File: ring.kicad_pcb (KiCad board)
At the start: 2 copper layers, 38 x 10 mm, 29 parts, among them J1 5034800240, J2 5034800440, Q1 IRLML6344TRPBF, U1 ANNA-B112-02B, U2 LSM6DSV16X

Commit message: Mark flex zone in board; fill BOM MPNs; honest status notes
- Draw the flex-zone boundary + fab note on User.Drawings in ring.kicad_pcb
- Fill the 9 TBD passive MPNs (Yageo RC0402 / Murata GRM15)
- README: prototype status, accurate DRC (0 errors; 2 minor VBAT warnings),
  and note that the rigid-flex stackup is left to the fabricator

Co-Authored-By: Claude Opus 4.8 (1M context) <noreply@anthropic.com>
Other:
- board text added: "FLEX"
- board text added: "FLEX ZONE x=18-26mm (8mm wide) - rigid-flex bend ~115deg, folds in housing"
- board text added: "rigid 1.0mm / flex core 0.1mm - rigid-flex stackup + coverlay to be defined by fab"
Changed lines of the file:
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@@
 	)
 	(embedded_fonts no)
+	(gr_line (start 18.0 -1.5) (end 18.0 11.5)
+		(stroke (width 0.12) (type dash)) (layer "Dwgs.User"))
+	(gr_line (start 26.0 -1.5) (end 26.0 11.5)
+		(stroke (width 0.12) (type dash)) (layer "Dwgs.User"))
+	(gr_text "FLEX"
+		(at 22.0 -2.6 0) (layer "Dwgs.User")
+		(effects (font (size 1.2 1.2) (thickness 0.15)) (justify left)))
+	(gr_text "FLEX ZONE  x=18-26mm (8mm wide) - rigid-flex bend ~115deg, folds in housing"
+		(at 0.0 13.0 0) (layer "Dwgs.User")
+		(effects (font (size 0.9 0.9) (thickness 0.15)) (justify left)))
+	(gr_text "rigid 1.0mm / flex core 0.1mm - rigid-flex stackup + coverlay to be defined by fab"
+		(at 0.0 14.6 0) (layer "Dwgs.User")
+		(effects (font (size 0.9 0.9) (thickness 0.15)) (justify left)))
 )

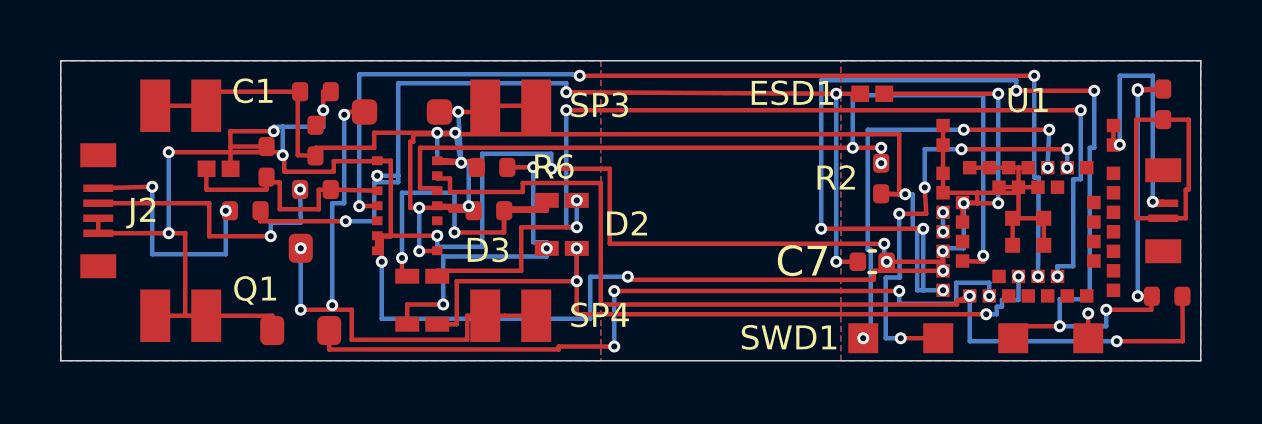
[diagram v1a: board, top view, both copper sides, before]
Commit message: Normalize ring board to DRC-clean
Drop a redundant near-stacked VBAT via (hole_to_hole) and a dangling B.Cu
stub + the via it orphaned (track_dangling), via the khalkeus normalize
pass. Connectivity unchanged; KiCad DRC now 0 errors / 0 warnings.
Regenerate the previews and update the status note.

Co-Authored-By: Claude Opus 4.8 (1M context) <noreply@anthropic.com>
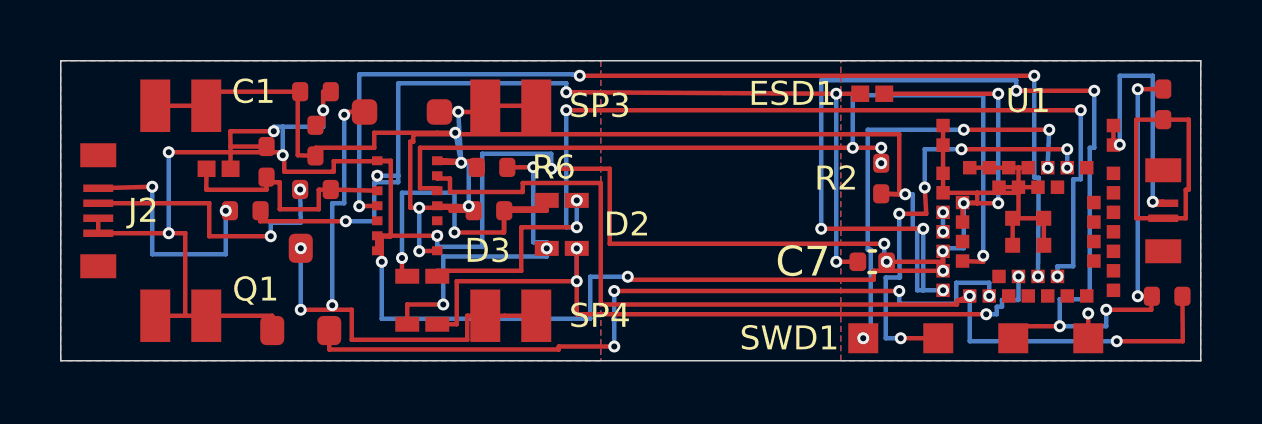
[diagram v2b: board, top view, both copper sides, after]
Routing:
- net VBAT: track 103.8 -> 102.0 mm, vias 18 -> 16
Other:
- board text removed: "FLEX"
- board text removed: "FLEX ZONE x=18-26mm (8mm wide) - rigid-flex bend ~115deg, folds in housing"
- board text removed: "rigid 1.0mm / flex core 0.1mm - rigid-flex stackup + coverlay to be defined by fab"
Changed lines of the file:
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@@
-	)
-	(segment
-		(start 35.9 1)
-		(end 36.75 0.9428)
-		(width 0.15)
-		(layer "F.Cu")
-		(net 3)
 	)
 	(segment
@@
 	)
 	(via
-		(at 12.55 2.4)
-		(size 0.4)
-		(drill 0.2)
-		(layers "F.Cu" "B.Cu")
-		(net 3)
-	)
-	(via
 		(at 34.45 1)
 		(size 0.4)
@@
 	(via
 		(at 11.95 4.9)
-		(size 0.4)
-		(drill 0.2)
-		(layers "F.Cu" "B.Cu")
-		(net 3)
-	)
-	(via
-		(at 35.9 1)
 		(size 0.4)
 		(drill 0.2)
@@
 		(start 34.45 2.9)
 		(end 34.3 2.9)
-		(width 0.15)
-		(layer "B.Cu")
-		(net 3)
-	)
-	(segment
-		(start 12.55 3.3328)
-		(end 12.55 2.4)
 		(width 0.15)
 		(layer "B.Cu")
@@
 	)
 	(embedded_fonts no)
-	(gr_line (start 18.0 -1.5) (end 18.0 11.5)
-		(stroke (width 0.12) (type dash)) (layer "Dwgs.User"))
-	(gr_line (start 26.0 -1.5) (end 26.0 11.5)
-		(stroke (width 0.12) (type dash)) (layer "Dwgs.User"))
-	(gr_text "FLEX"
-		(at 22.0 -2.6 0) (layer "Dwgs.User")
-		(effects (font (size 1.2 1.2) (thickness 0.15)) (justify left)))
-	(gr_text "FLEX ZONE  x=18-26mm (8mm wide) - rigid-flex bend ~115deg, folds in housing"
-		(at 0.0 13.0 0) (layer "Dwgs.User")
-		(effects (font (size 0.9 0.9) (thickness 0.15)) (justify left)))
-	(gr_text "rigid 1.0mm / flex core 0.1mm - rigid-flex stackup + coverlay to be defined by fab"
-		(at 0.0 14.6 0) (layer "Dwgs.User")
-		(effects (font (size 0.9 0.9) (thickness 0.15)) (justify left)))
 )

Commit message: Fix bi-color LED miswire; re-solve clean (0 DRC / 0 parity)
The LEDs (D2/D3) were miswired: the net-to-pad assignment was scrambled,
so the green die had both terminals on VBAT (dead) and the red die was
GPIO-to-GPIO with no current limit. The board was DRC-clean, so it
looked fine -- but it was electrically broken, and the schematic was 111
parity-issues out of sync with the PCB.

- corrected LED net mapping (re-solved on the fixed netlist)
- schematic now matches the PCB exactly: 0 schematic-parity issues
  (symbol pin numbers = footprint pad names; global, slash-free labels)
- vias 0.4 -> 0.3mm (0.15mm drill) so the LSM6DSV16X's 0.5mm-pitch
  escapes clear the 0.127mm rule -> 0 DRC
- bom: add R8 (100k Q1 gate pull-down -- prevents uncommanded motor run
  on a floating gate at boot/reset)
- regenerated fab/ gerbers + drill, schematic PDF, board preview
- readme: honest flex-zone note (structural zoning, not a board layer)

Verified in KiCad 9: 0 DRC errors, 0 unconnected, 0 schematic-parity.

Co-Authored-By: Claude Opus 4.8 (1M context) <noreply@anthropic.com>
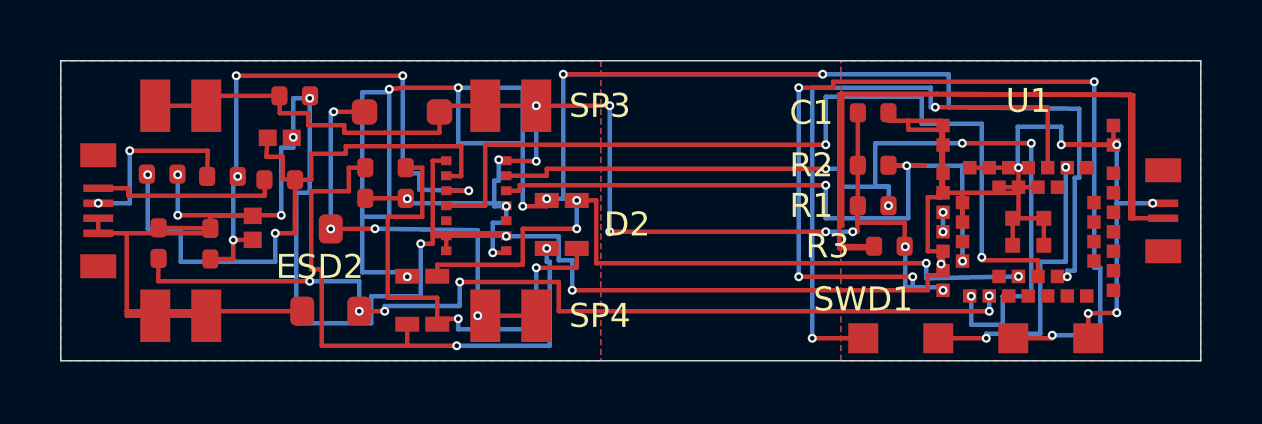
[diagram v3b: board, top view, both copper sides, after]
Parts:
- added R8: 100k, R_0402_1005Metric, F.Cu at (3.26, 6.08)
- C7: value C7 -> 110pF; footprint C_0402_1005Metric -> R_0402_1005Metric
- moved C7 23.8 mm to (3.38, 3.78)
- moved ESD1 19.8 mm to (7.30, 2.57)
- moved C1 18.6 mm to (27.1, 1.73)
- moved R3 10.3 mm to (27.6, 6.18), turned to 0 degrees
- moved R1 10.3 mm to (27.1, 4.83)
- moved R7 4.23 mm to (10.2, 4.08), turned to 90 degrees
- moved C8 3.31 mm to (4.99, 6.10)
- moved R5 3.13 mm to (5.39, 3.86)
- moved R6 2.92 mm to (11.5, 4.08), turned to 90 degrees
- moved U2 2.30 mm to (13.8, 4.83)
- moved ESD2 2.28 mm to (6.40, 5.57), turned to 90 degrees
- moved C2 1.64 mm to (7.80, 1.17), turned to 0 degrees
- moved R4 1.54 mm to (7.30, 3.97)
- moved Q1 1.19 mm to (9.00, 6.98)
- moved R2 0.52 mm to (27.1, 3.48), turned to 0 degrees
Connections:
- D2 pad GA: LED_RED_A -> LED_GREEN_A
- D2 pad GK: LED_GREEN_A -> LED_GREEN
- D2 pad RA: LED_RED -> LED_RED_A
- D2 pad RK: LED_GREEN -> LED_RED
- D3 pad GA: LED_RED_A -> LED_GREEN_A
- D3 pad GK: LED_GREEN_A -> LED_GREEN
- D3 pad RA: LED_RED -> LED_RED_A
- D3 pad RK: LED_GREEN -> LED_RED
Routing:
- net VBUS: track 10.1 -> 40.7 mm
- net LED_GREEN: track 34.9 -> 65.1 mm, vias 5 -> 8
- net VBAT: track 102.0 -> 84.4 mm, vias 16 -> 17
- net QVAR2: track 8.55 -> 20.2 mm, vias 0 -> 5
- net QVAR1: track 32.3 -> 21.0 mm, vias 5 -> 2
- net GND: track 119.9 -> 110.2 mm, vias 19 -> 15
- net LED_GREEN_A: track 12.4 -> 19.7 mm
- net SCL: track 30.2 -> 23.9 mm, vias 4 -> 3
- net SWDIO: track 14.6 -> 20.6 mm, vias 4 -> 2
- net HAPTIC_EN: track 26.1 -> 31.9 mm, vias 4 -> 6
- net LED_RED_A: track 11.2 -> 16.3 mm, vias 3 -> 2
- net IMU_INT: track 34.3 -> 29.3 mm, vias 4 -> 2
- net SWDCLK: track 14.8 -> 9.95 mm, vias 6 -> 2
- net MOTOR_N: track 19.4 -> 14.7 mm
- net SDA: track 33.5 -> 30.3 mm, vias 2 -> 5
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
